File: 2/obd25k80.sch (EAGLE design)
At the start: 56 parts, among them IC1 PIC18F25K80, IC2 MCP2562, IC3 78L05, IC4 78L05, IC5 LE33CZ, J1 MA04-1, J2 DB9-M, Q1 BC547, Q2 BC557, Q3 BC547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

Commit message: Cleanup
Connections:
- net RA5 renamed C2INB
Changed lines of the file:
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@@
 <setting verticaltext="up"/>
 </settings>
-<grid distance="0.1" unitdist="inch" unit="inch" style="lines" multiple="1" display="yes" altdistance="0.01" altunitdist="inch" altunit="inch"/>
+<grid distance="0.1" unitdist="inch" unit="inch" style="lines" multiple="1" display="no" altdistance="0.01" altunitdist="inch" altunit="inch"/>
 <layers>
 <layer number="1" name="Top" color="4" fill="1" visible="no" active="no"/>
@@
 </segment>
 </net>
-<net name="RA5" class="0">
+<net name="C2INB" class="0">
 <segment>
 <pinref part="IC1" gate="G$1" pin="C2INB"/>

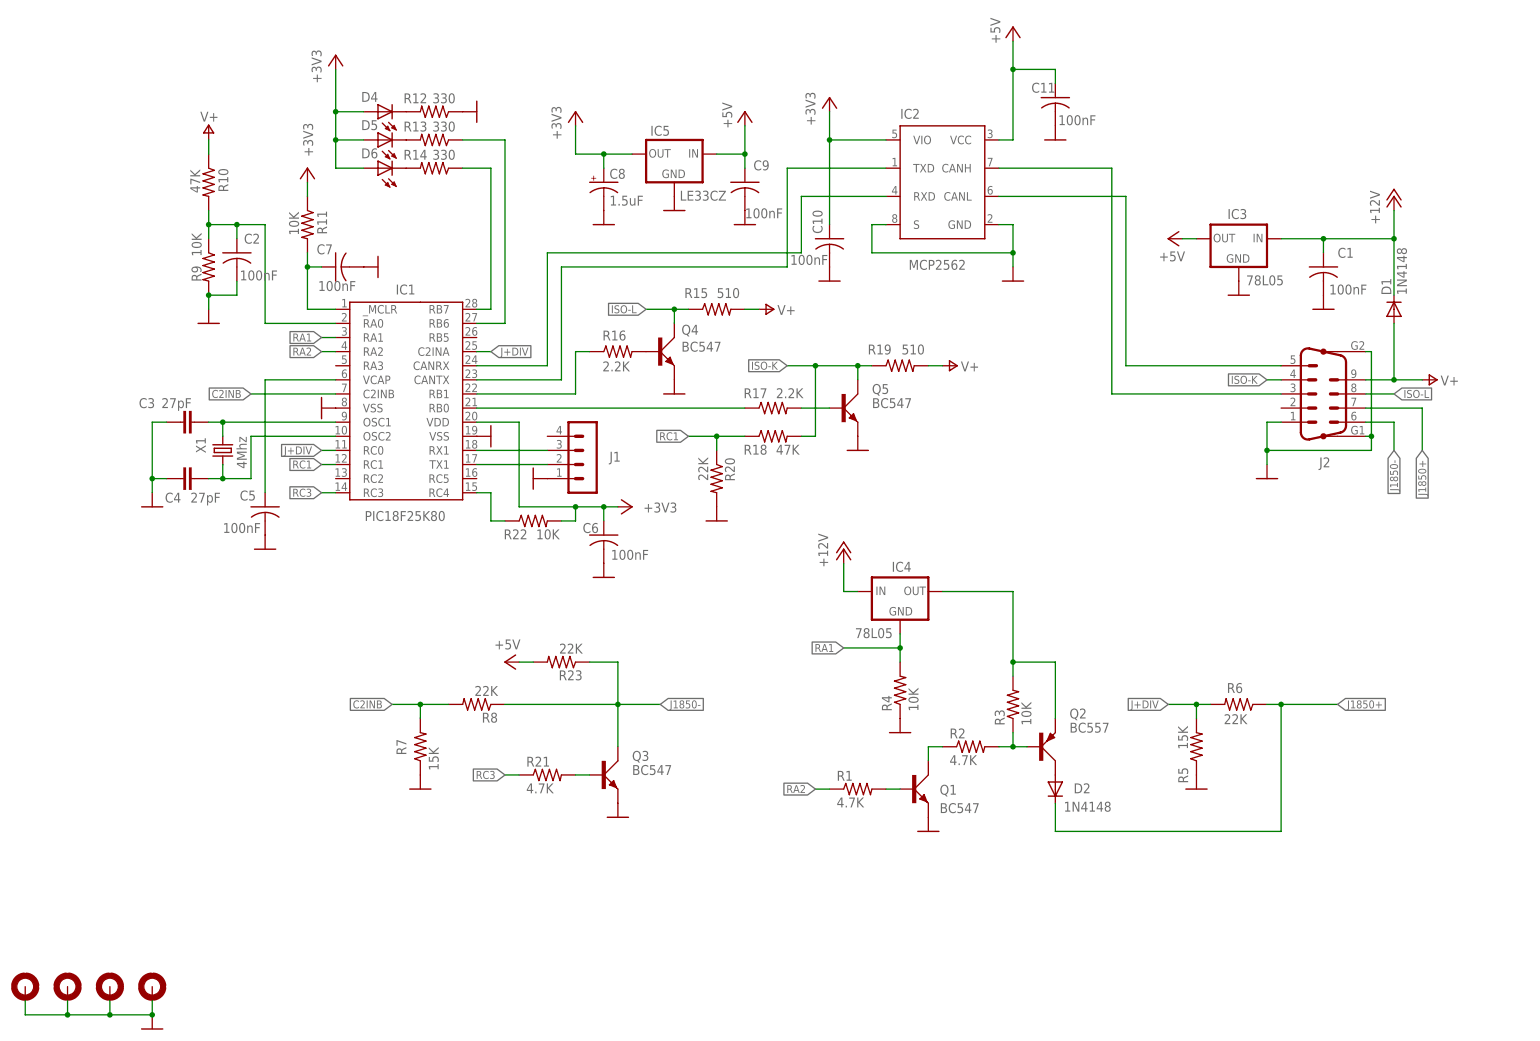
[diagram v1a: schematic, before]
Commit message: Reimplemented with ULN2003
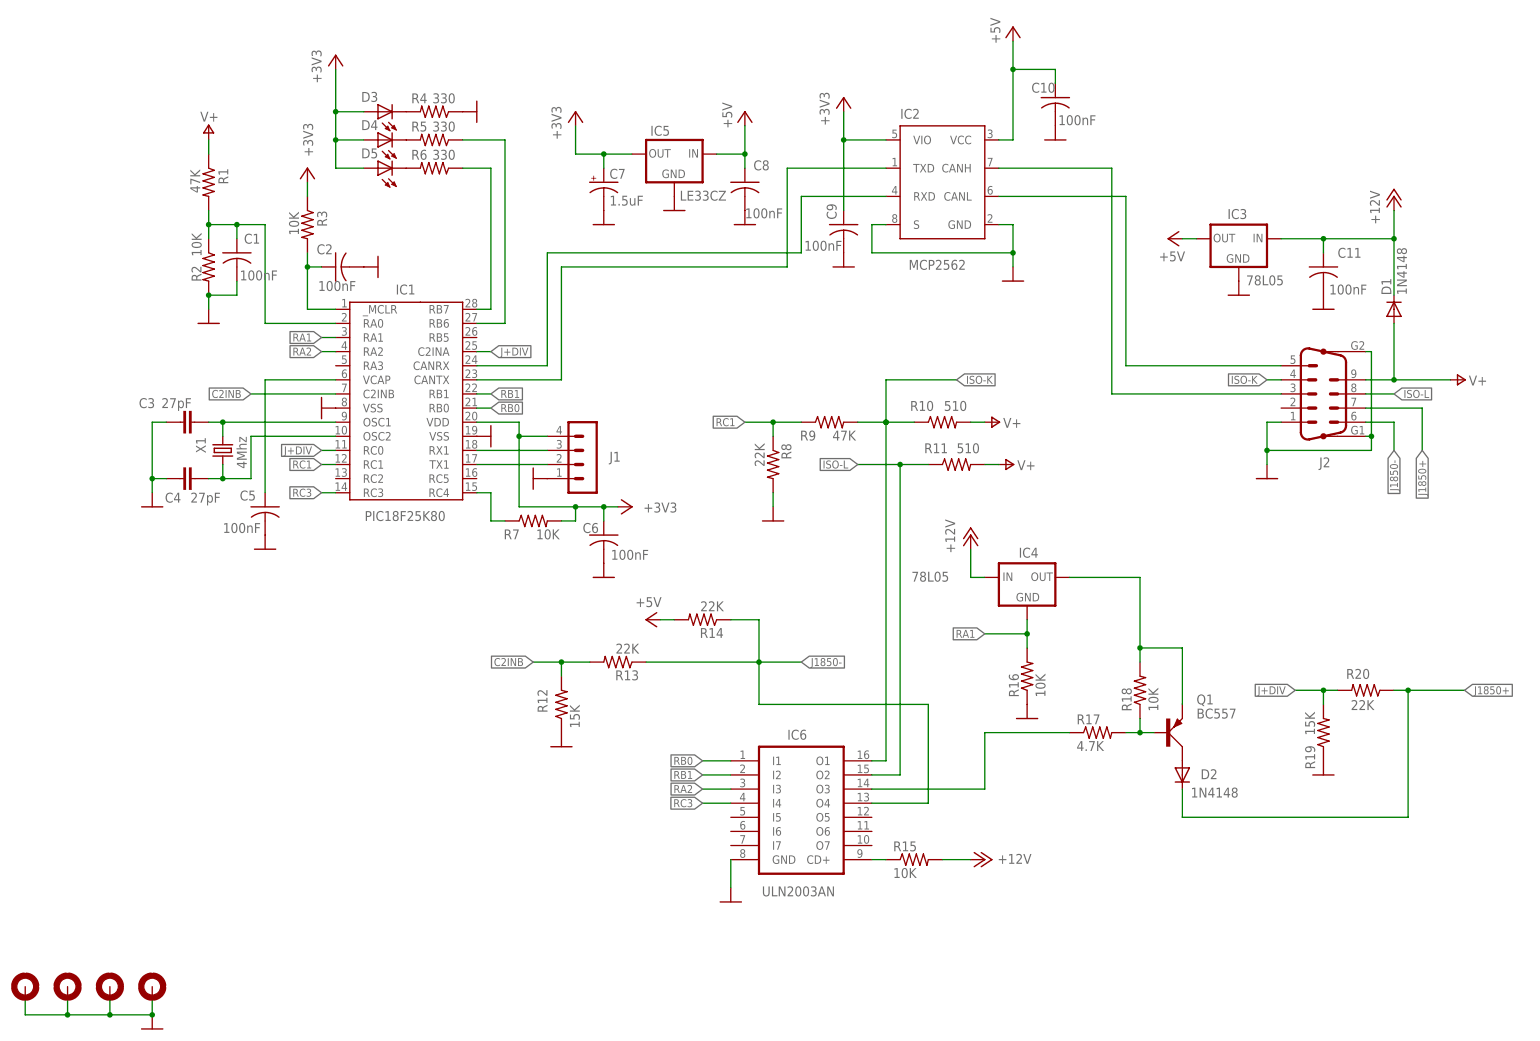
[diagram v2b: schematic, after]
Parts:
- removed D6: (no value), led:LED5MM
- removed Q2: BC557, transistor-small-signal:BC557
- removed Q3, Q4, Q5: BC547, transistor-small-signal:BC547
- removed R21: 4.7K, rcl:R-US_0207/10
- removed R22: 10K, rcl:R-US_0207/10
- removed R23: 22K, rcl:R-US_0207/10
- added D3: (no value), led:LED5MM
- added IC6: ULN2003AN, uln-udn:ULN2003AN
- C7: value 100nF -> 1.5uF; device rcl:C-US050-025X075 -> rcl:CPOL-USE2.5-5
- C8: value 1.5uF -> 100nF; device rcl:CPOL-USE2.5-5 -> rcl:C-US050-025X075
- Q1: value BC547 -> BC557; device transistor-small-signal:BC547 -> transistor-small-signal:BC557
- R1: value 4.7K -> 47K
- R10: value 47K -> 510
- R11: value 10K -> 510
- R12: value 330 -> 15K
- R13, R14: value 330 -> 22K
- R15: value 510 -> 10K
- R16: value 2.2K -> 10K
- R17: value 2.2K -> 4.7K
- R18: value 47K -> 10K
- R19: value 510 -> 15K
- R2: value 4.7K -> 10K
- R4: value 10K -> 330
- R5: value 15K -> 330
- R6: value 22K -> 330
- R7: value 15K -> 10K
- R9: value 10K -> 47K
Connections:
- removed net N$15: Q4.B, R16.2
- removed net N$20: IC1.RB0, R17.1
- removed net N$22: Q3.B, R21.2
- removed net N$24: Q5.B, R17.2
- removed net N$28: Q1.B, R1.2
- removed net N$9: IC1.RB1, R16.1
- new net N$4: IC6.CD+, R15.1
- new net RB0: IC1.RB0, IC6.I1
- new net RB1: IC1.RB1, IC6.I2
- net +12V: now also C11.1, R15.2; no longer C1.1
- net +3V3: now also C7.+, C9.1, D3.A, J1.4, R3.1, R7.2; no longer C10.1, C8.+, D6.A, R11.1, R22.2
- net +5V: now also C10.1, C8.1, R14.2; no longer C11.1, C9.1, R23.2
- net C2INB: now also R12.2, R13.2; no longer R7.2, R8.2
- net GND: now also C7.-, C8.2, IC6.GND, R16.1, R19.1, R2.2, R8.2; no longer C7.2, C8.-, Q1.E, Q3.E, Q4.E, Q5.E, R20.2, R5.1, R7.1, R9.2
- net ISO-K: now also IC6.O1, R10.1, R9.2; no longer Q5.C, R18.2, R19.1
- net ISO-L: now also IC6.O2, R11.1; no longer Q4.C, R15.1
- net J+DIV: now also R19.2, R20.2; no longer R5.2, R6.2
- net J1850+: now also R20.1; no longer R6.1
- net J1850-: now also IC6.O4, R13.1, R14.1; no longer Q3.C, R23.1, R8.1
- net N$1: now also D3.C, R4.2; no longer D4.C, R12.2
- net N$10: now also D5.C, R6.2; no longer D6.C, R14.2
- net N$11: now also R5.1; no longer R13.1
- net N$2: now also R6.1; no longer R14.1
- net N$25: now also IC6.O3, R17.1; no longer Q1.C, R2.1
- net N$26: now also C1.1, R1.2, R2.1; no longer C2.1, R10.2, R9.1
- net N$3: now also R7.1; no longer R22.1
- net N$30: now also Q1.B, R17.2, R18.1; no longer Q2.B, R2.2, R3.1
- net N$31: now also Q1.E, R18.2; no longer Q2.E, R3.2
- net N$32: now also Q1.C; no longer Q2.C
- net N$6: now also D4.C, R5.2; no longer D5.C, R13.2
- net N$7: now also C2.1, R3.2; no longer C7.1, R11.2
- net RA1: now also R16.2; no longer R4.2
- net RA2: now also IC6.I3; no longer R1.1
- net RC1: now also R8.1, R9.1; no longer R18.1, R20.1
- net RC3: now also IC6.I4; no longer R21.1
- net V+: now also R1.1, R10.2, R11.2; no longer R10.1, R15.2, R19.2
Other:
- moved on the sheet: C1, C10, C11, C2, C9, D2, D4, D5, IC4, Q1, R1, R10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

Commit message: Another 3.3V LDO
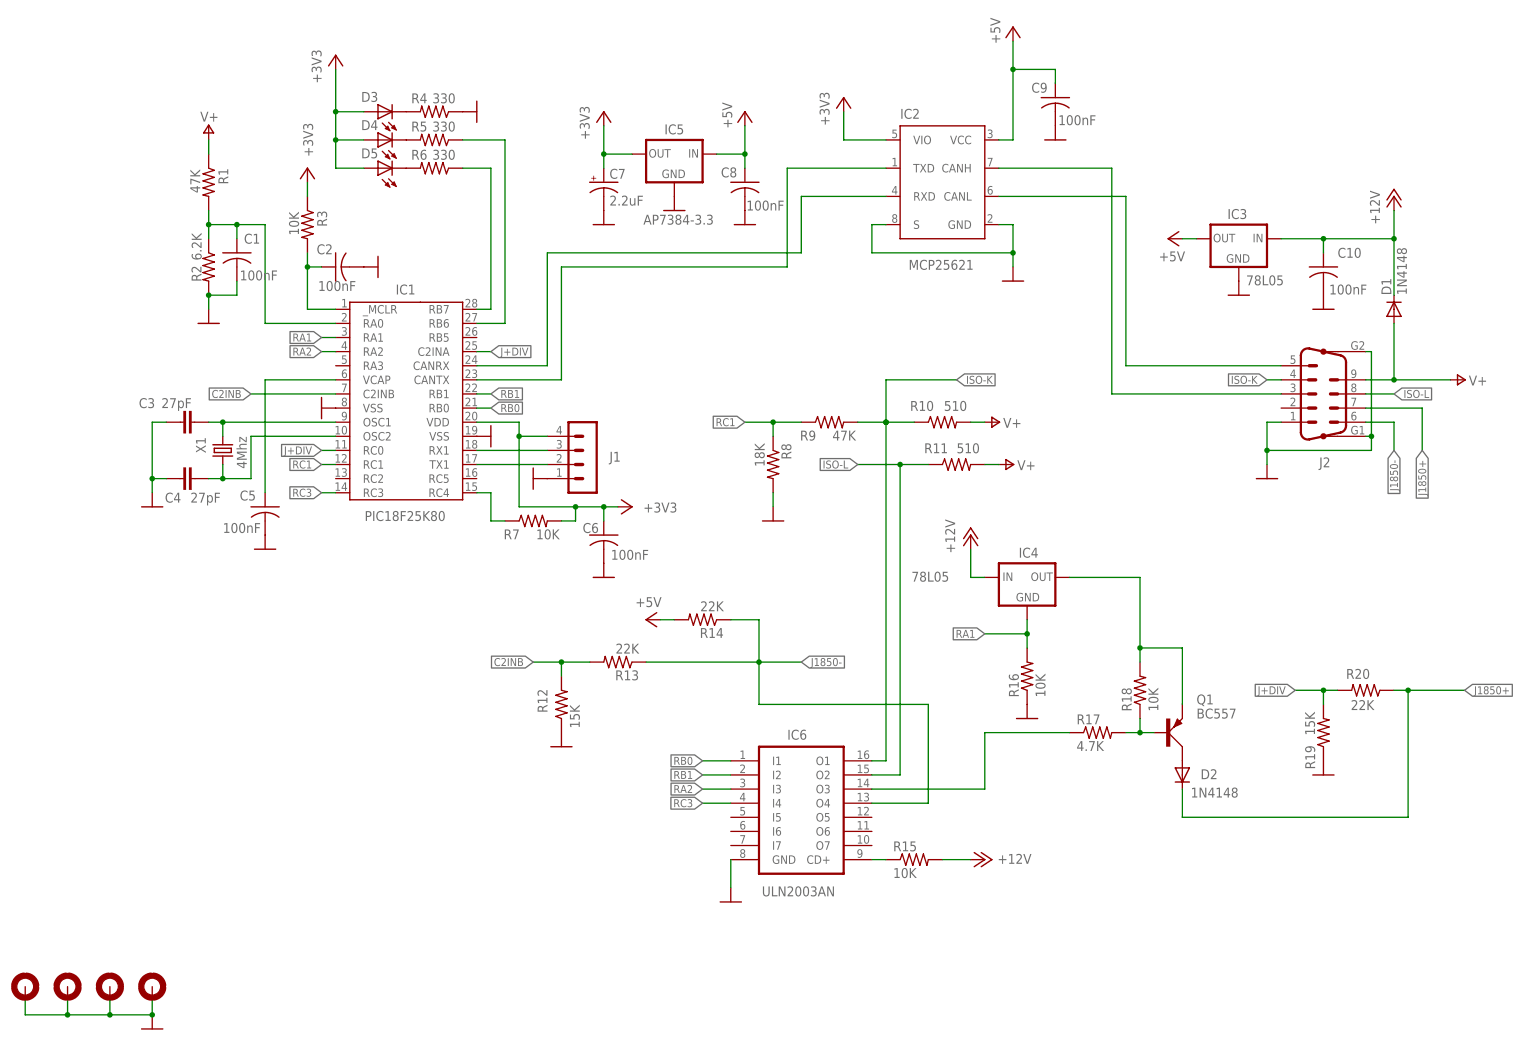
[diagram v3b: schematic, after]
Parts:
- removed C11: 100nF, rcl:C-US050-025X075
- C7: value 1.5uF -> 2.2uF
- IC2: value MCP2562 -> MCP25621; device obddiag-net:MCP2562 -> obddiag-net:MCP25621
- IC5: value LE33CZ -> AP7384-3.3; device v-reg:78LXX -> obddiag-net:AP7384
- R2: value 10K -> 6.2K
- R8: value 22K -> 18K
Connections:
- net +12V: now also C10.1; no longer C11.1
- net +3V3: no longer C9.1
- net +5V: now also C9.1; no longer C10.1
- net GND: no longer C11.2
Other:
- moved on the sheet: C10, C9

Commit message: Updated with resistor arrays
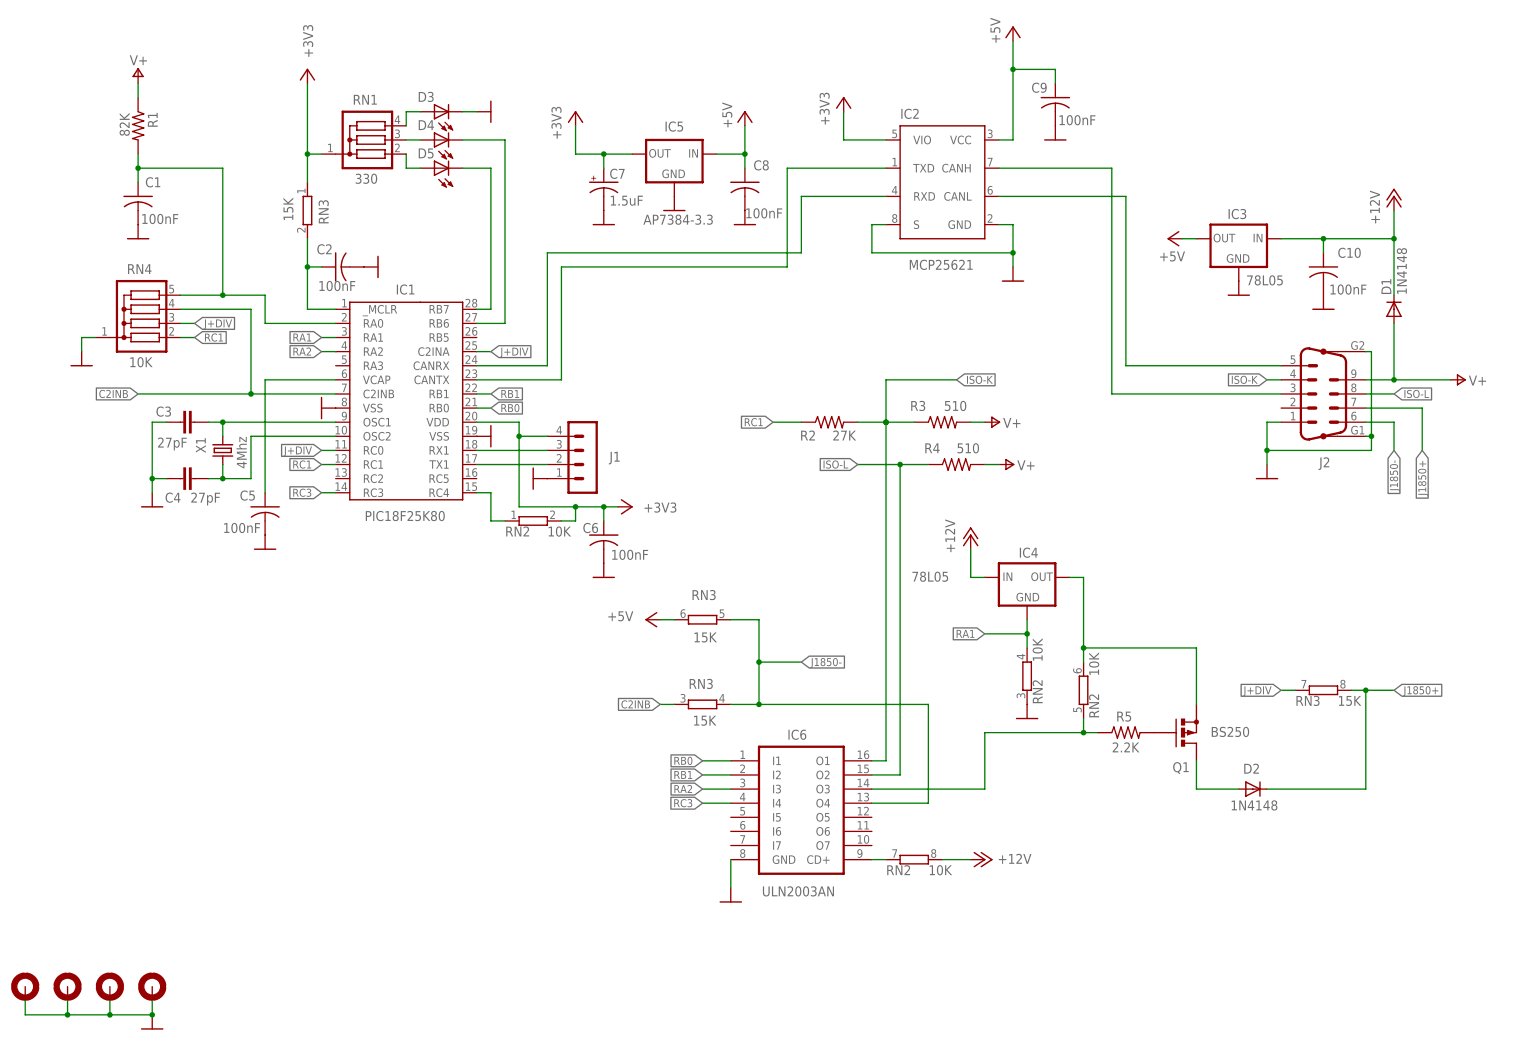
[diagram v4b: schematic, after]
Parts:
- removed R10, R11: 510, rcl:R-US_0207/10
- removed R12, R19: 15K, rcl:R-US_0207/10
- removed R13, R14, R20: 22K, rcl:R-US_0207/10
- removed R15, R16, R18, R7: 10K, rcl:R-US_0207/10
- removed R17: 4.7K, rcl:R-US_0207/10
- removed R6: 330, rcl:R-US_0207/10
- removed R8: 18K, rcl:R-US_0207/10
- removed R9: 47K, rcl:R-US_0207/10
- added RN1: 330, resistor-sil:G03R
- added RN2: 10K, resistor-sil:E4RP
- added RN3: 15K, resistor-sil:E4RP
- added RN4: 10K, resistor-sil:G04R
- C7: value 2.2uF -> 1.5uF
- Q1: value BC557 -> BS250; device transistor-small-signal:BC557 -> transistor-small-signal:BS250
- R1: value 47K -> 82K
- R2: value 6.2K -> 27K
- R3: value 10K -> 510
- R4: value 330 -> 510
- R5: value 330 -> 2.2K
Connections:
- removed net N$26: C1.1, IC1.RA0, R1.2, R2.1
- removed net N$30: Q1.B, R17.2, R18.1
- removed net N$32: D2.A, Q1.C
- new net N$5: D4.A, RN1.3
- new net N$8: D2.A, Q1.D
- new net N$9: C1.1, IC1.RA0, R1.2, RN4.5
- net +12V: now also RN2D.2; no longer R15.2
- net +3V3: now also RN1.1, RN2A.2, RN3A.1; no longer D3.A, D4.A, D5.A, R3.1, R7.2
- net +5V: now also RN3C.2; no longer R14.2
- net C2INB: now also RN3B.1, RN4.4; no longer R12.2, R13.2
- net GND: now also D3.C, RN2B.1, RN4.1; no longer R12.1, R16.1, R19.1, R2.2, R4.1, R8.2
- net ISO-K: now also R2.2, R3.1; no longer R10.1, R9.2
- net ISO-L: now also R4.1; no longer R11.1
- net J+DIV: now also RN3D.1, RN4.3; no longer R19.2, R20.2
- net J1850+: now also RN3D.2; no longer R20.1
- net J1850-: now also RN3B.2, RN3C.1; no longer R13.1, R14.1
- net N$1: now also D5.A, RN1.2; no longer D3.C, R4.2
- net N$10: now also Q1.G, R5.2; no longer D5.C, R6.2
- net N$11: now also D4.C; no longer R5.1
- net N$2: now also D5.C; no longer R6.1
- net N$25: now also R5.1, RN2C.1; no longer R17.1
- net N$3: now also RN2A.1; no longer R7.1
- net N$31: now also Q1.S, RN2C.2; no longer Q1.E, R18.2
- net N$4: now also RN2D.1; no longer R15.1
- net N$6: now also D3.A, RN1.4; no longer D4.C, R5.2
- net N$7: now also RN3A.2; no longer R3.2
- net RA1: now also RN2B.2; no longer R16.2
- net RC1: now also R2.1, RN4.2; no longer R8.1, R9.1
- net V+: now also R3.2, R4.2; no longer R10.2, R11.2
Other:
- moved on the sheet: C1, D2, D3, D4, D5, R1, R2, R3, R4, R5
